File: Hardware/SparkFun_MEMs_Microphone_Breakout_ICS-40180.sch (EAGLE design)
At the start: 14 parts, among them U1 OPA344, U2 ICS40180

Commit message: changed label to fish flag output on AUD pin
added fiducials
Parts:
- added FD1, FD2, FD3, FD4: FIDUCIALUFIDUCIAL, SparkFun-Aesthetics:FIDUCIALUFIDUCIAL
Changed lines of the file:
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@@
 <part name="LOGO2" library="SparkFun-Aesthetics" deviceset="OSHW-LOGO" device="MINI"/>
 <part name="FRAME2" library="SparkFun-Aesthetics" deviceset="FRAME-LETTER" device=""/>
+<part name="FD1" library="SparkFun-Aesthetics" deviceset="FIDUCIAL" device="UFIDUCIAL"/>
+<part name="FD2" library="SparkFun-Aesthetics" deviceset="FIDUCIAL" device="UFIDUCIAL"/>
+<part name="FD3" library="SparkFun-Aesthetics" deviceset="FIDUCIAL" device="UFIDUCIAL"/>
+<part name="FD4" library="SparkFun-Aesthetics" deviceset="FIDUCIAL" device="UFIDUCIAL"/>
 </parts>
 <sheets>
@@
 <attribute name="REV" x="236.22" y="6.604" size="2.7432" layer="94" font="vector"/>
 </instance>
+<instance part="FD1" gate="G$1" x="241.3" y="40.64" smashed="yes"/>
+<instance part="FD2" gate="G$1" x="243.84" y="40.64" smashed="yes"/>
+<instance part="FD3" gate="G$1" x="243.84" y="38.1" smashed="yes"/>
+<instance part="FD4" gate="G$1" x="241.3" y="38.1" smashed="yes"/>
 </instances>
 <busses>

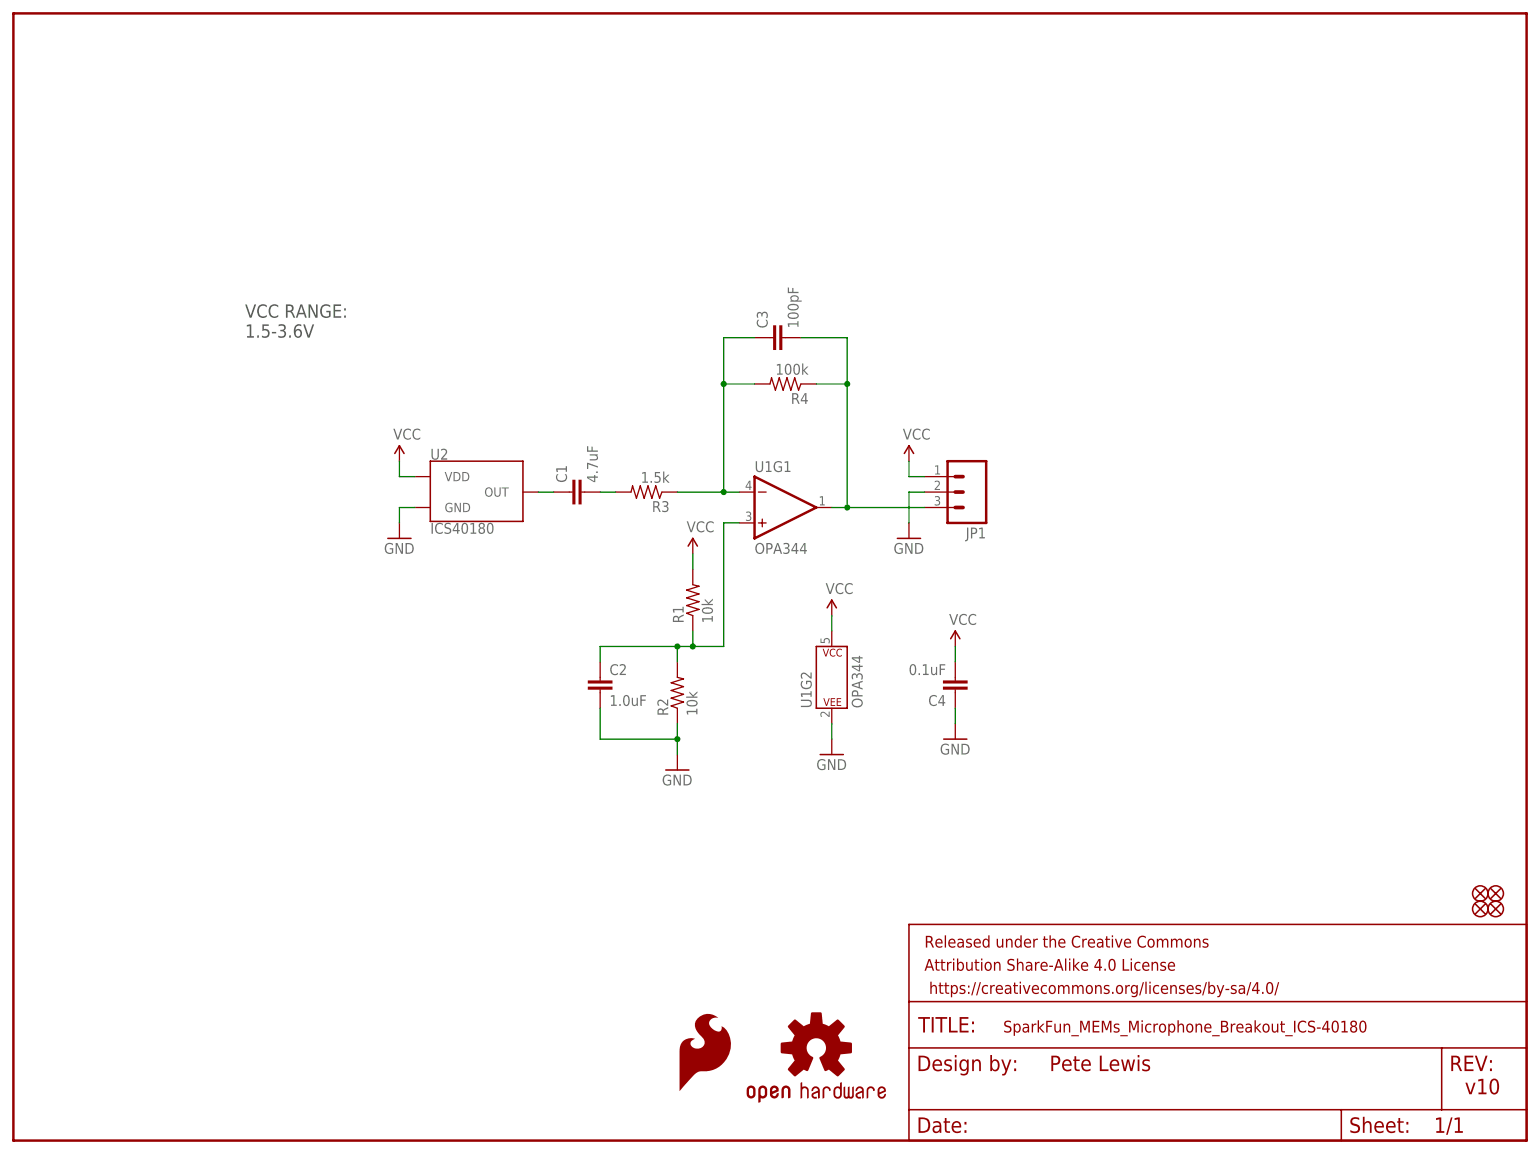
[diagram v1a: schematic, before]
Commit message: Changed values to extend freq response
-Changes passives to extend frequency rolloffs on the opamp circuit. It's not 7.2Hz-19.7KHz, which better matches the capabilities of the new mic.
-Added SparkFun "name" logo to schematic - note, I copied vectors from library so it isn't a proper symbol/device.
-rearranged schematic and labeled "mic" and "gainstage" sections
-Capitalized the S in MEMS on the bottom silk.
-Made measures text size all the same at 0.05inch
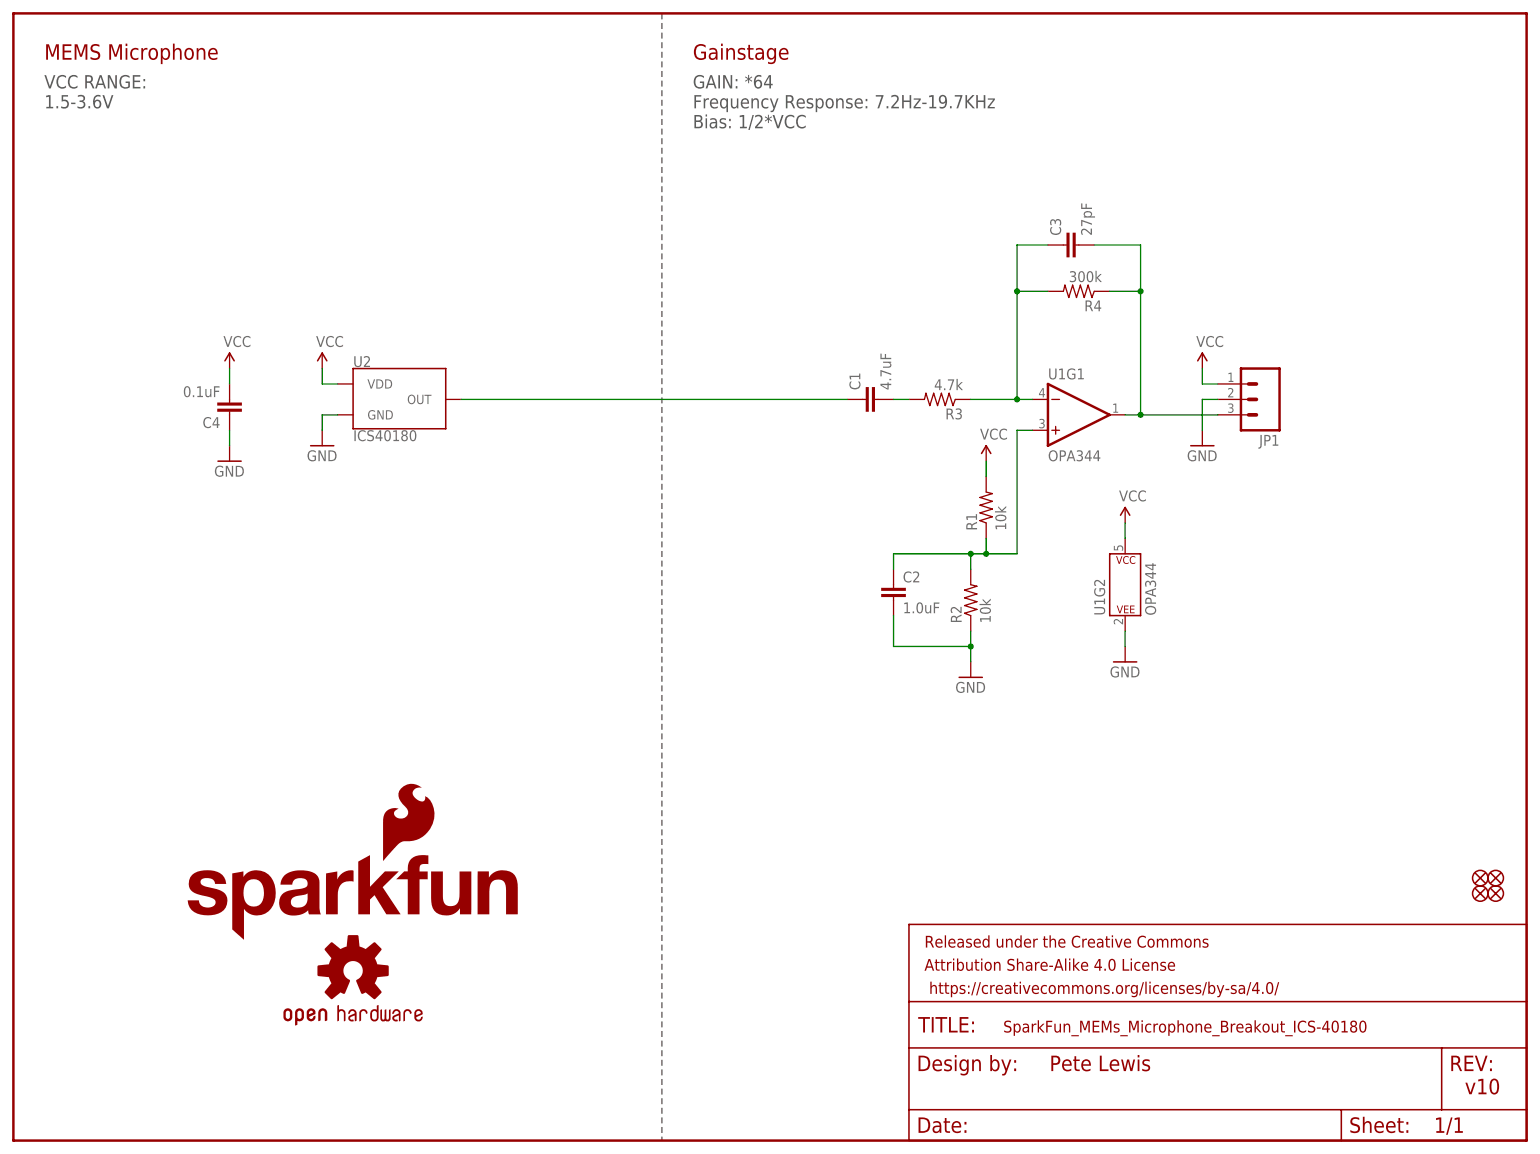
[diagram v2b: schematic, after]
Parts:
- C3: value 100pF -> 27pF; device SparkFun-Capacitors:100PF-0603-50V-5% -> SparkFun-Capacitors:27PF-0603-50V-5%
- R3: value 1.5k -> 4.7k; device SparkFun-Resistors:1.5KOHM-0603-1/10W-1% -> SparkFun-Resistors:4.7KOHM-0603-1/10W-1%
- R4: value 100k -> 300k; device SparkFun-Resistors:100KOHM-0603-1/10W-1% -> SparkFun-Resistors:300KOHM-0603-1/10W-1%
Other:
- note added: "GAIN: *64 Frequency Response: 7.2Hz-19.7KHz Bias: 1/2*VCC"
- note added: "Gainstage"
- note added: "MEMS Microphone"
- moved on the sheet: C1, C2, C3, C4, JP1, R1, R2, R3, R4, U1G1, U1G2, U2
